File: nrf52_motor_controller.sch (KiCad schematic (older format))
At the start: 50 parts, among them J1 Screw_Terminal_01x04, J2 Conn_01x12, J3 Conn_01x12, Q1 AO3400A, SW1 SW_Push, SW2 SW_Push, U1 HT7533, U2 nRF52832-QFAA, U3 DRV8876PWPT, Y1 32MHz, Y2 32.768kHz

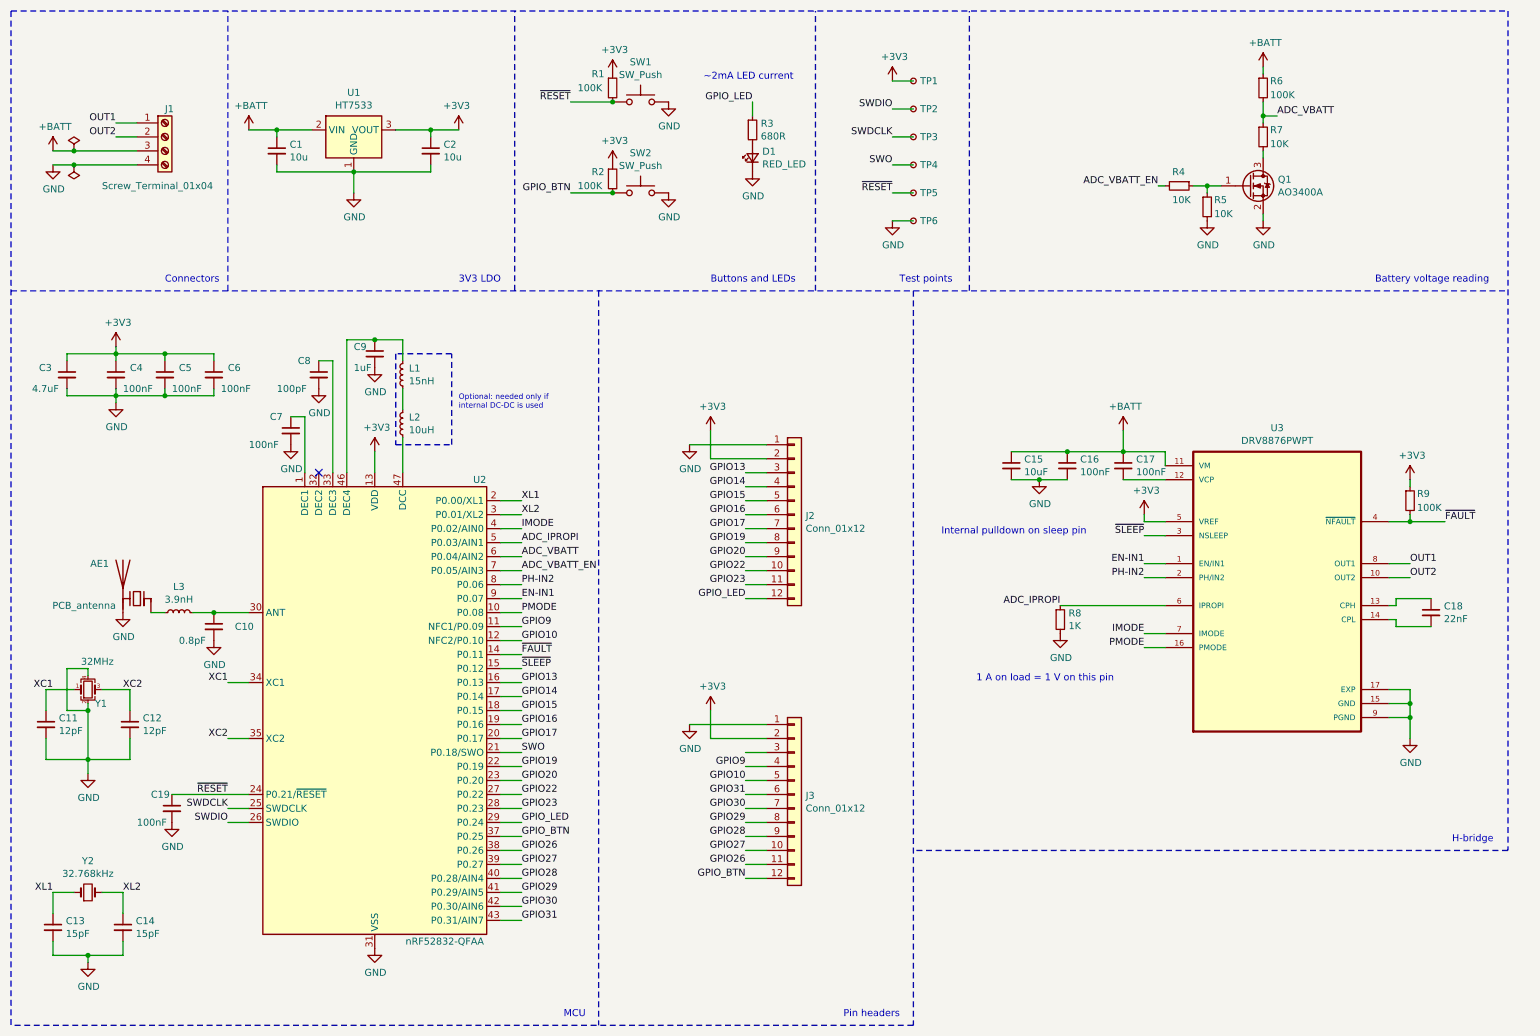
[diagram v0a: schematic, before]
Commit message: Replace 12 pin headers with 10 pin
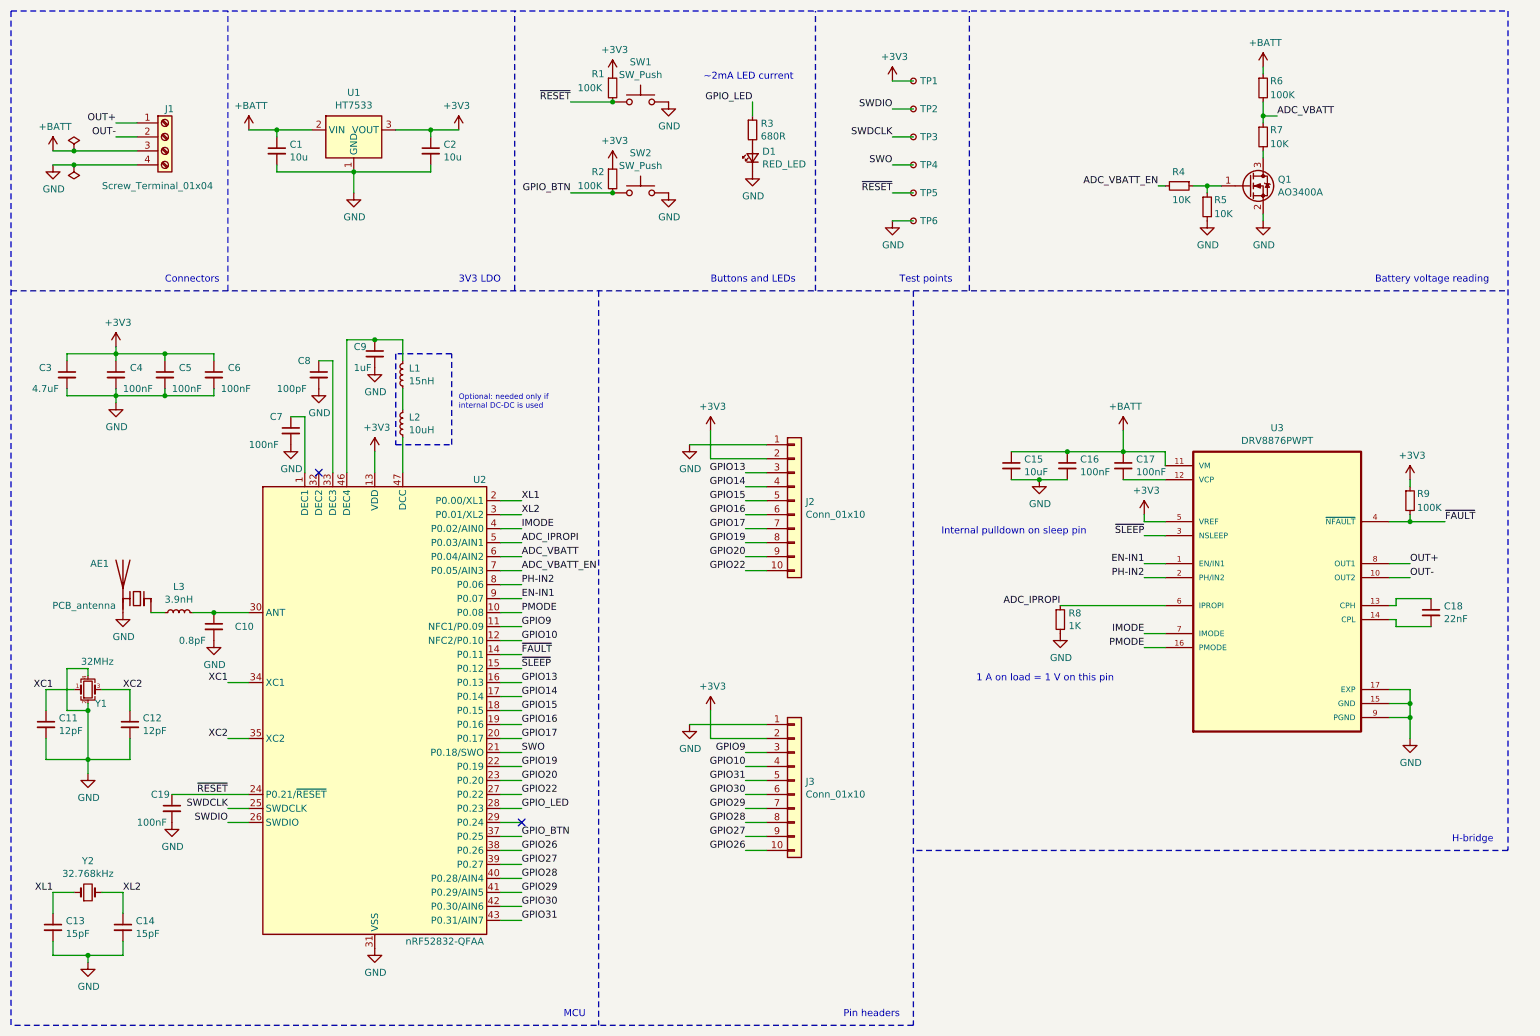
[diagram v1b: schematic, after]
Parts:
- removed J2, J3: Conn_01x12, Connector_PinHeader_2.54mm:PinHeader_1x12_P2.54mm_Vertical, symbol Connector_Generic:Conn_01x12
- added J2, J3: Conn_01x10, Connector_PinHeader_2.54mm:PinHeader_1x10_P2.54mm_Vertical, symbol Connector_Generic:Conn_01x10
- AE1: footprint RF_Antenna:Texas_SWRA117D_2.4GHz_Right -> RF_Antenna:Texas_SWRA117D_2.4GHz_Left
- R1, R2: footprint Resistor_SMD:R_0603_1608Metric -> Resistor_SMD:R_0402_1005Metric
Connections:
- net GPIO23 is gone; now on net GPIO_LED: U2.28 (P0.23)
- net +3V3: now also J2.2 (Pin_2), J3.2 (Pin_2)
- net GND: now also J2.1 (Pin_1), J3.1 (Pin_1)
- net GPIO10: now also J3.4 (Pin_4)
- net GPIO13: now also J2.3 (Pin_3)
- net GPIO14: now also J2.4 (Pin_4)
- net GPIO15: now also J2.5 (Pin_5)
- net GPIO16: now also J2.6 (Pin_6)
- net GPIO17: now also J2.7 (Pin_7)
- net GPIO19: now also J2.8 (Pin_8)
- net GPIO20: now also J2.9 (Pin_9)
- net GPIO22: now also J2.10 (Pin_10)
- net GPIO26: now also J3.10 (Pin_10)
- net GPIO27: now also J3.9 (Pin_9)
- net GPIO28: now also J3.8 (Pin_8)
- net GPIO29: now also J3.7 (Pin_7)
- net GPIO30: now also J3.6 (Pin_6)
- net GPIO31: now also J3.5 (Pin_5)
- net GPIO9: now also J3.3 (Pin_3)
- net GPIO_LED: no longer U2.29 (P0.24)
- net OUT1 renamed OUT+
- net OUT2 renamed OUT-
- no-connect marks 1 -> 2
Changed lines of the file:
@@
 ~FAULT
 Text Label 10500 4450 0    50   ~ 0
-OUT1
+OUT+
 Text Label 10500 4550 0    50   ~ 0
-OUT2
+OUT-
 $Comp
 L power:GND #PWR?
@@
 F 0 "R2" H 4650 1750 50  0000 L CNN
 F 1 "100K" H 4550 1650 50  0000 L CNN
-F 2 "Resistor_SMD:R_0603_1608Metric" H 4800 1700 50  0001 C CNN
+F 2 "Resistor_SMD:R_0402_1005Metric" H 4800 1700 50  0001 C CNN
 F 3 "https://datasheet.lcsc.com/lcsc/2206010100_UNI-ROYAL-Uniroyal-Elec-0603WAF6800T5E_C23228.pdf" H 4800 1700 50  0001 C CNN
 F 4 "C23228" H 4800 1700 50  0001 C CNN "LCSC"
@@
 F 0 "R1" H 4650 1150 50  0000 L CNN
 F 1 "100K" H 4550 1050 50  0000 L CNN
-F 2 "Resistor_SMD:R_0603_1608Metric" H 4800 1050 50  0001 C CNN
+F 2 "Resistor_SMD:R_0402_1005Metric" H 4800 1050 50  0001 C CNN
 F 3 "https://datasheet.lcsc.com/lcsc/2206010100_UNI-ROYAL-Uniroyal-Elec-0603WAF6800T5E_C23228.pdf" H 4800 1050 50  0001 C CNN
 F 4 "C23228" H 4800 1050 50  0001 C CNN "LCSC"
@@
 Test points
 Text Label 1250 1300 2    50   ~ 0
-OUT1
+OUT+
 Text Label 1250 1400 2    50   ~ 0
-OUT2
+OUT-
 Wire Wire Line
 	1250 1300 1400 1300
@@
 F 0 "AE1" H 1600 4950 50  0000 L CNN
 F 1 "PCB_antenna" H 1550 4650 50  0000 L CNN
-F 2 "RF_Antenna:Texas_SWRA117D_2.4GHz_Right" H 1300 4875 50  0001 C CNN
+F 2 "RF_Antenna:Texas_SWRA117D_2.4GHz_Left" H 1300 4875 50  0001 C CNN
 F 3 "~" H 1300 4875 50  0001 C CNN
 	1    1400 4700
@@
 Wire Wire Line
 	4150 4500 4000 4500
-Text Label 4150 6300 0    50   ~ 0
+Text Label 4150 6200 0    50   ~ 0
 GPIO_LED
 Wire Wire Line
@@
 Wire Notes Line
 	6950 2500 6950 7750
-$Comp
-L Connector_Generic:Conn_01x12 J2
-U 1 1 63944AEA
-P 6100 4100
-F 0 "J2" H 6180 4092 50  0000 L CNN
-F 1 "Conn_01x12" H 6180 4001 50  0000 L CNN
-F 2 "Connector_PinHeader_2.54mm:PinHeader_1x12_P2.54mm_Vertical" H 6100 4100 50  0001 C CNN
-F 3 "~" H 6100 4100 50  0001 C CNN
-	1    6100 4100
-	1    0    0    -1
-$EndComp
-$Comp
-L Connector_Generic:Conn_01x12 J3
-U 1 1 63945246
-P 6100 6100
-F 0 "J3" H 6180 6092 50  0000 L CNN
-F 1 "Conn_01x12" H 6180 6001 50  0000 L CNN
-F 2 "Connector_PinHeader_2.54mm:PinHeader_1x12_P2.54mm_Vertical" H 6100 6100 50  0001 C CNN
-F 3 "~" H 6100 6100 50  0001 C CNN
-	1    6100 6100
-	1    0    0    -1
-$EndComp
 Wire Wire Line
 	4000 4200 4150 4200
@@
 Text Label 4150 6100 0    50   ~ 0
 GPIO22
-Text Label 4150 6200 0    50   ~ 0
-GPIO23
 Text Label 4150 6500 0    50   ~ 0
 GPIO26
@@
 	5900 4500 5750 4500
 Wire Wire Line
-	5900 4600 5750 4600
-Wire Wire Line
-	5900 4700 5750 4700
-Wire Wire Line
 	5900 5800 5750 5800
 Wire Wire Line
@@
 Wire Wire Line
 	5900 6500 5750 6500
-Wire Wire Line
-	5900 6600 5750 6600
-Wire Wire Line
-	5900 6700 5750 6700
+Text Label 5750 6000 2    50   ~ 0
+GPIO31
 Text Label 5750 6100 2    50   ~ 0
-GPIO31
+GPIO30
 Text Label 5750 6200 2    50   ~ 0
-GPIO30
+GPIO29
 Text Label 5750 6300 2    50   ~ 0
-GPIO29
+GPIO28
 Text Label 5750 6400 2    50   ~ 0
-GPIO28
+GPIO27
 Text Label 5750 6500 2    50   ~ 0
-GPIO27
-Text Label 5750 6600 2    50   ~ 0
 GPIO26
-Text Label 5750 6700 2    50   ~ 0
-GPIO_BTN
-Text Label 5750 4700 2    50   ~ 0
-GPIO_LED
-Text Label 5750 4600 2    50   ~ 0
-GPIO23
 Text Label 5750 4500 2    50   ~ 0
 GPIO22
@@
 Text Label 5750 3800 2    50   ~ 0
 GPIO13
-Text Label 5750 6000 2    50   ~ 0
+Text Label 5750 5900 2    50   ~ 0
 GPIO10
 Text Label 4150 4600 0    50   ~ 0
@@
 Text Label 4150 4200 0    50   ~ 0
 IMODE
-Text Label 5750 5900 2    50   ~ 0
+Text Label 5750 5800 2    50   ~ 0
 GPIO9
 Text Label 9550 1250 0    50   ~ 0
@@
 Wire Wire Line
 	1650 6100 2200 6100
+$Comp
+L Connector_Generic:Conn_01x10 J3
+U 1 1 63BD5321
+P 6100 6000
+F 0 "J3" H 6180 5992 50  0000 L CNN
+F 1 "Conn_01x10" H 6180 5901 50  0000 L CNN
+F 2 "Connector_PinHeader_2.54mm:PinHeader_1x10_P2.54mm_Vertical" H 6100 6000 50  0001 C CNN
+F 3 "~" H 6100 6000 50  0001 C CNN
+	1    6100 6000
+	1    0    0    -1
+$EndComp
+NoConn ~ 4150 6300
+$Comp
+L Connector_Generic:Conn_01x10 J2
+U 1 1 63C344E1
+P 6100 4000
+F 0 "J2" H 6180 3992 50  0000 L CNN
+F 1 "Conn_01x10" H 6180 3901 50  0000 L CNN
+F 2 "Connector_PinHeader_2.54mm:PinHeader_1x10_P2.54mm_Vertical" H 6100 4000 50  0001 C CNN
+F 3 "~" H 6100 4000 50  0001 C CNN
+	1    6100 4000
+	1    0    0    -1
+$EndComp
 $EndSCHEMATC

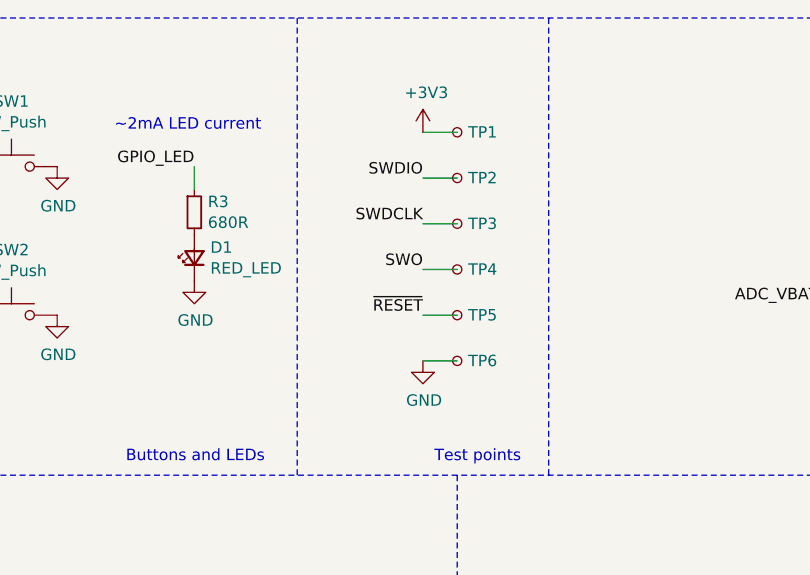
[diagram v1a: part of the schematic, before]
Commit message: Add custom test point symbol and footprint for 1.27 mm pitch TP
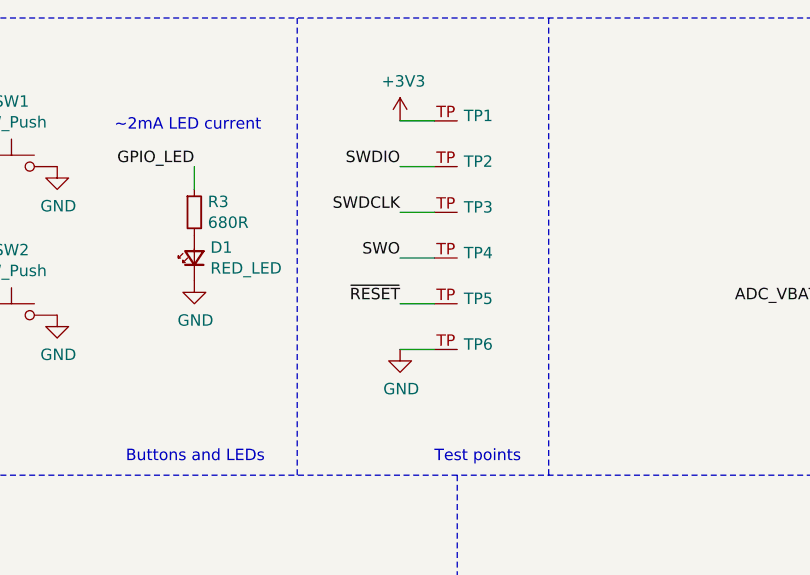
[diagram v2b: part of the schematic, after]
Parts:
- removed TP1: VTref, TestPoint:TestPoint_Pad_D1.0mm, symbol Connector:TestPoint_Small
- removed TP2: SWDIO, TestPoint:TestPoint_Pad_D1.0mm, symbol Connector:TestPoint_Small
- removed TP3: SWDCLK, TestPoint:TestPoint_Pad_D1.0mm, symbol Connector:TestPoint_Small
- removed TP4: SWO, TestPoint:TestPoint_Pad_D1.0mm, symbol Connector:TestPoint_Small
- removed TP5: ~RESET, TestPoint:TestPoint_Pad_D1.0mm, symbol Connector:TestPoint_Small
- removed TP6: GND, TestPoint:TestPoint_Pad_D1.0mm, symbol Connector:TestPoint_Small
- added TP1, TP2, TP3, TP4, TP5, TP6: Test_point_1mm, custom_footprints:test_point_1mm, symbol custom_symbols:Test_point_1mm
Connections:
- net +3V3: now also TP1.TP
- net GND: now also TP6.TP
- net SWDCLK: now also TP3.TP
- net SWDIO: now also TP2.TP
- net SWO: now also TP4.TP
- net ~RESET: now also TP5.TP
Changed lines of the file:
@@
 Internal pulldown on sleep pin
-$Comp
-L Connector:TestPoint_Small TP?
-U 1 1 63908BB4
-P 6950 1000
-AR Path="/637E70BB/63908BB4" Ref="TP?"  Part="1"
-AR Path="/63908BB4" Ref="TP1"  Part="1"
-F 0 "TP1" H 6998 1000 50  0000 L CNN
-F 1 "VTref" H 6998 955 50  0001 L CNN
-F 2 "TestPoint:TestPoint_Pad_D1.0mm" H 7150 1000 50  0001 C CNN
-F 3 "~" H 7150 1000 50  0001 C CNN
-	1    6950 1000
-	1    0    0    -1
-$EndComp
-$Comp
-L Connector:TestPoint_Small TP?
-U 1 1 63908BBA
-P 6950 1200
-AR Path="/637E70BB/63908BBA" Ref="TP?"  Part="1"
-AR Path="/63908BBA" Ref="TP2"  Part="1"
-F 0 "TP2" H 6998 1200 50  0000 L CNN
-F 1 "SWDIO" H 6998 1155 50  0001 L CNN
-F 2 "TestPoint:TestPoint_Pad_D1.0mm" H 7150 1200 50  0001 C CNN
-F 3 "~" H 7150 1200 50  0001 C CNN
-	1    6950 1200
-	1    0    0    -1
-$EndComp
-$Comp
-L Connector:TestPoint_Small TP?
-U 1 1 63908BC0
-P 6950 1400
-AR Path="/637E70BB/63908BC0" Ref="TP?"  Part="1"
-AR Path="/63908BC0" Ref="TP3"  Part="1"
-F 0 "TP3" H 6998 1400 50  0000 L CNN
-F 1 "SWDCLK" H 6998 1355 50  0001 L CNN
-F 2 "TestPoint:TestPoint_Pad_D1.0mm" H 7150 1400 50  0001 C CNN
-F 3 "~" H 7150 1400 50  0001 C CNN
-	1    6950 1400
-	1    0    0    -1
-$EndComp
-$Comp
-L Connector:TestPoint_Small TP?
-U 1 1 63908BC6
-P 6950 1600
-AR Path="/637E70BB/63908BC6" Ref="TP?"  Part="1"
-AR Path="/63908BC6" Ref="TP4"  Part="1"
-F 0 "TP4" H 6998 1600 50  0000 L CNN
-F 1 "SWO" H 6998 1555 50  0001 L CNN
-F 2 "TestPoint:TestPoint_Pad_D1.0mm" H 7150 1600 50  0001 C CNN
-F 3 "~" H 7150 1600 50  0001 C CNN
-	1    6950 1600
-	1    0    0    -1
-$EndComp
-$Comp
-L Connector:TestPoint_Small TP?
-U 1 1 63908BCC
-P 6950 1800
-AR Path="/637E70BB/63908BCC" Ref="TP?"  Part="1"
-AR Path="/63908BCC" Ref="TP5"  Part="1"
-F 0 "TP5" H 6998 1800 50  0000 L CNN
-F 1 "~RESET" H 6998 1754 50  0001 L CNN
-F 2 "TestPoint:TestPoint_Pad_D1.0mm" H 7150 1800 50  0001 C CNN
-F 3 "~" H 7150 1800 50  0001 C CNN
-	1    6950 1800
-	1    0    0    -1
-$EndComp
-$Comp
-L Connector:TestPoint_Small TP?
-U 1 1 63908BD2
-P 6950 2000
-AR Path="/637E70BB/63908BD2" Ref="TP?"  Part="1"
-AR Path="/63908BD2" Ref="TP6"  Part="1"
-F 0 "TP6" H 6998 2000 50  0000 L CNN
-F 1 "GND" H 6998 1955 50  0001 L CNN
-F 2 "TestPoint:TestPoint_Pad_D1.0mm" H 7150 2000 50  0001 C CNN
-F 3 "~" H 7150 2000 50  0001 C CNN
-	1    6950 2000
-	1    0    0    -1
-$EndComp
-Text Label 6800 1200 2    50   ~ 0
-SWDIO
-Wire Wire Line
-	6950 1000 6800 1000
-Wire Wire Line
-	6950 1200 6800 1200
-Wire Wire Line
-	6950 1400 6800 1400
-Wire Wire Line
-	6950 1600 6800 1600
-Wire Wire Line
-	6950 1800 6800 1800
-Wire Wire Line
-	6950 2000 6800 2000
-Text Label 6800 1400 2    50   ~ 0
-SWDCLK
-Text Label 6800 1600 2    50   ~ 0
-SWO
-Text Label 6800 1800 2    50   ~ 0
-~RESET
-$Comp
-L power:GND #PWR?
-U 1 1 63908BE2
-P 6800 2000
-AR Path="/637E70BB/63908BE2" Ref="#PWR?"  Part="1"
-AR Path="/63908BE2" Ref="#PWR023"  Part="1"
-F 0 "#PWR023" H 6800 1750 50  0001 C CNN
-F 1 "GND" H 6805 1827 50  0000 C CNN
-F 2 "" H 6800 2000 50  0001 C CNN
-F 3 "" H 6800 2000 50  0001 C CNN
-	1    6800 2000
-	1    0    0    -1
-$EndComp
-$Comp
-L power:+3V3 #PWR?
-U 1 1 63908BE8
-P 6800 1000
-AR Path="/637E70BB/63908BE8" Ref="#PWR?"  Part="1"
-AR Path="/63908BE8" Ref="#PWR022"  Part="1"
-F 0 "#PWR022" H 6800 850 50  0001 C CNN
-F 1 "+3V3" H 6815 1173 50  0000 C CNN
-F 2 "" H 6800 1000 50  0001 C CNN
-F 3 "" H 6800 1000 50  0001 C CNN
-	1    6800 1000
-	1    0    0    -1
-$EndComp
 $Comp
 L Device:LED_Small D?
@@
 	1    0    0    -1
 $EndComp
+$Comp
+L power:+3V3 #PWR?
+U 1 1 63DEDDD7
+P 6700 950
+AR Path="/637E70BB/63DEDDD7" Ref="#PWR?"  Part="1"
+AR Path="/63DEDDD7" Ref="#PWR034"  Part="1"
+F 0 "#PWR034" H 6700 800 50  0001 C CNN
+F 1 "+3V3" H 6715 1123 50  0000 C CNN
+F 2 "" H 6700 950 50  0001 C CNN
+F 3 "" H 6700 950 50  0001 C CNN
+	1    6700 950
+	1    0    0    -1
+$EndComp
+Text Label 6700 1150 2    50   ~ 0
+SWDIO
+Text Label 6700 1350 2    50   ~ 0
+SWDCLK
+Text Label 6700 1550 2    50   ~ 0
+SWO
+Text Label 6700 1750 2    50   ~ 0
+~RESET
+$Comp
+L power:GND #PWR?
+U 1 1 63E08CF2
+P 6700 1950
+AR Path="/637E70BB/63E08CF2" Ref="#PWR?"  Part="1"
+AR Path="/63E08CF2" Ref="#PWR035"  Part="1"
+F 0 "#PWR035" H 6700 1700 50  0001 C CNN
+F 1 "GND" H 6705 1777 50  0000 C CNN
+F 2 "" H 6700 1950 50  0001 C CNN
+F 3 "" H 6700 1950 50  0001 C CNN
+	1    6700 1950
+	1    0    0    -1
+$EndComp
+Wire Wire Line
+	6700 1950 6850 1950
+Wire Wire Line
+	6700 1750 6850 1750
+Wire Wire Line
+	6700 1550 6850 1550
+Wire Wire Line
+	6700 1350 6850 1350
+Wire Wire Line
+	6700 1150 6850 1150
+Wire Wire Line
+	6700 950  6850 950
+$Comp
+L custom_symbols:Test_point_1mm TP1
+U 1 1 63F5A7C8
+P 6850 950
+F 0 "TP1" H 6979 972 50  0000 L CNN
+F 1 "Test_point_1mm" H 6900 850 50  0001 C CNN
+F 2 "custom_footprints:test_point_1mm" H 6850 1150 50  0001 C CNN
+F 3 "" H 6850 1150 50  0001 C CNN
+	1    6850 950
+	1    0    0    -1
+$EndComp
+$Comp
+L custom_symbols:Test_point_1mm TP2
+U 1 1 63F5AC4F
+P 6850 1150
+F 0 "TP2" H 6979 1172 50  0000 L CNN
+F 1 "Test_point_1mm" H 6900 1050 50  0001 C CNN
+F 2 "custom_footprints:test_point_1mm" H 6850 1350 50  0001 C CNN
+F 3 "" H 6850 1350 50  0001 C CNN
+	1    6850 1150
+	1    0    0    -1
+$EndComp
+$Comp
+L custom_symbols:Test_point_1mm TP3
+U 1 1 63F5AF4B
+P 6850 1350
+F 0 "TP3" H 6979 1372 50  0000 L CNN
+F 1 "Test_point_1mm" H 6900 1250 50  0001 C CNN
+F 2 "custom_footprints:test_point_1mm" H 6850 1550 50  0001 C CNN
+F 3 "" H 6850 1550 50  0001 C CNN
+	1    6850 1350
+	1    0    0    -1
+$EndComp
+$Comp
+L custom_symbols:Test_point_1mm TP4
+U 1 1 63F5B12D
+P 6850 1550
+F 0 "TP4" H 6979 1572 50  0000 L CNN
+F 1 "Test_point_1mm" H 6900 1450 50  0001 C CNN
+F 2 "custom_footprints:test_point_1mm" H 6850 1750 50  0001 C CNN
+F 3 "" H 6850 1750 50  0001 C CNN
+	1    6850 1550
+	1    0    0    -1
+$EndComp
+$Comp
+L custom_symbols:Test_point_1mm TP5
+U 1 1 63F5B3FE
+P 6850 1750
+F 0 "TP5" H 6979 1772 50  0000 L CNN
+F 1 "Test_point_1mm" H 6900 1650 50  0001 C CNN
+F 2 "custom_footprints:test_point_1mm" H 6850 1950 50  0001 C CNN
+F 3 "" H 6850 1950 50  0001 C CNN
+	1    6850 1750
+	1    0    0    -1
+$EndComp
+$Comp
+L custom_symbols:Test_point_1mm TP6
+U 1 1 63F5B68A
+P 6850 1950
+F 0 "TP6" H 6979 1972 50  0000 L CNN
+F 1 "Test_point_1mm" H 6900 1850 50  0001 C CNN
+F 2 "custom_footprints:test_point_1mm" H 6850 2150 50  0001 C CNN
+F 3 "" H 6850 2150 50  0001 C CNN
+	1    6850 1950
+	1    0    0    -1
+$EndComp
